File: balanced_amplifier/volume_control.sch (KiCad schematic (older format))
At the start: 49 parts, among them U5 LM4562, U6 LM4562, U7 LM4562, U8 LM4562

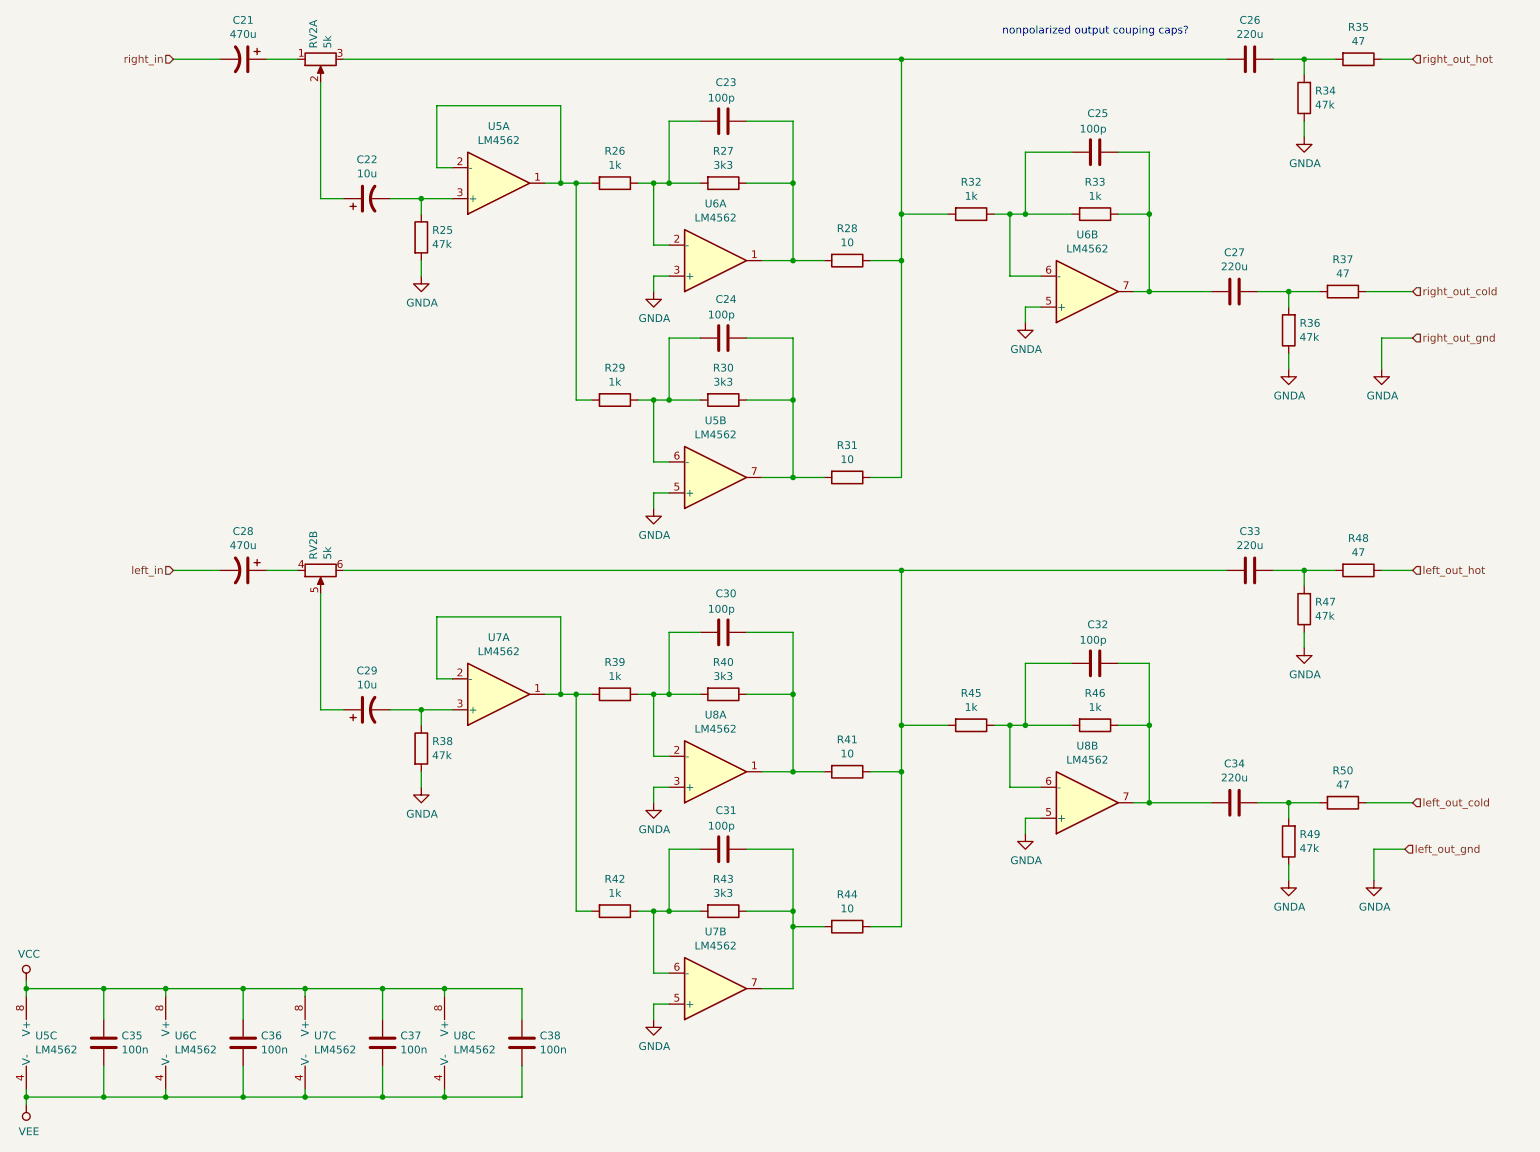
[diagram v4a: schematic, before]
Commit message: Add testpoints
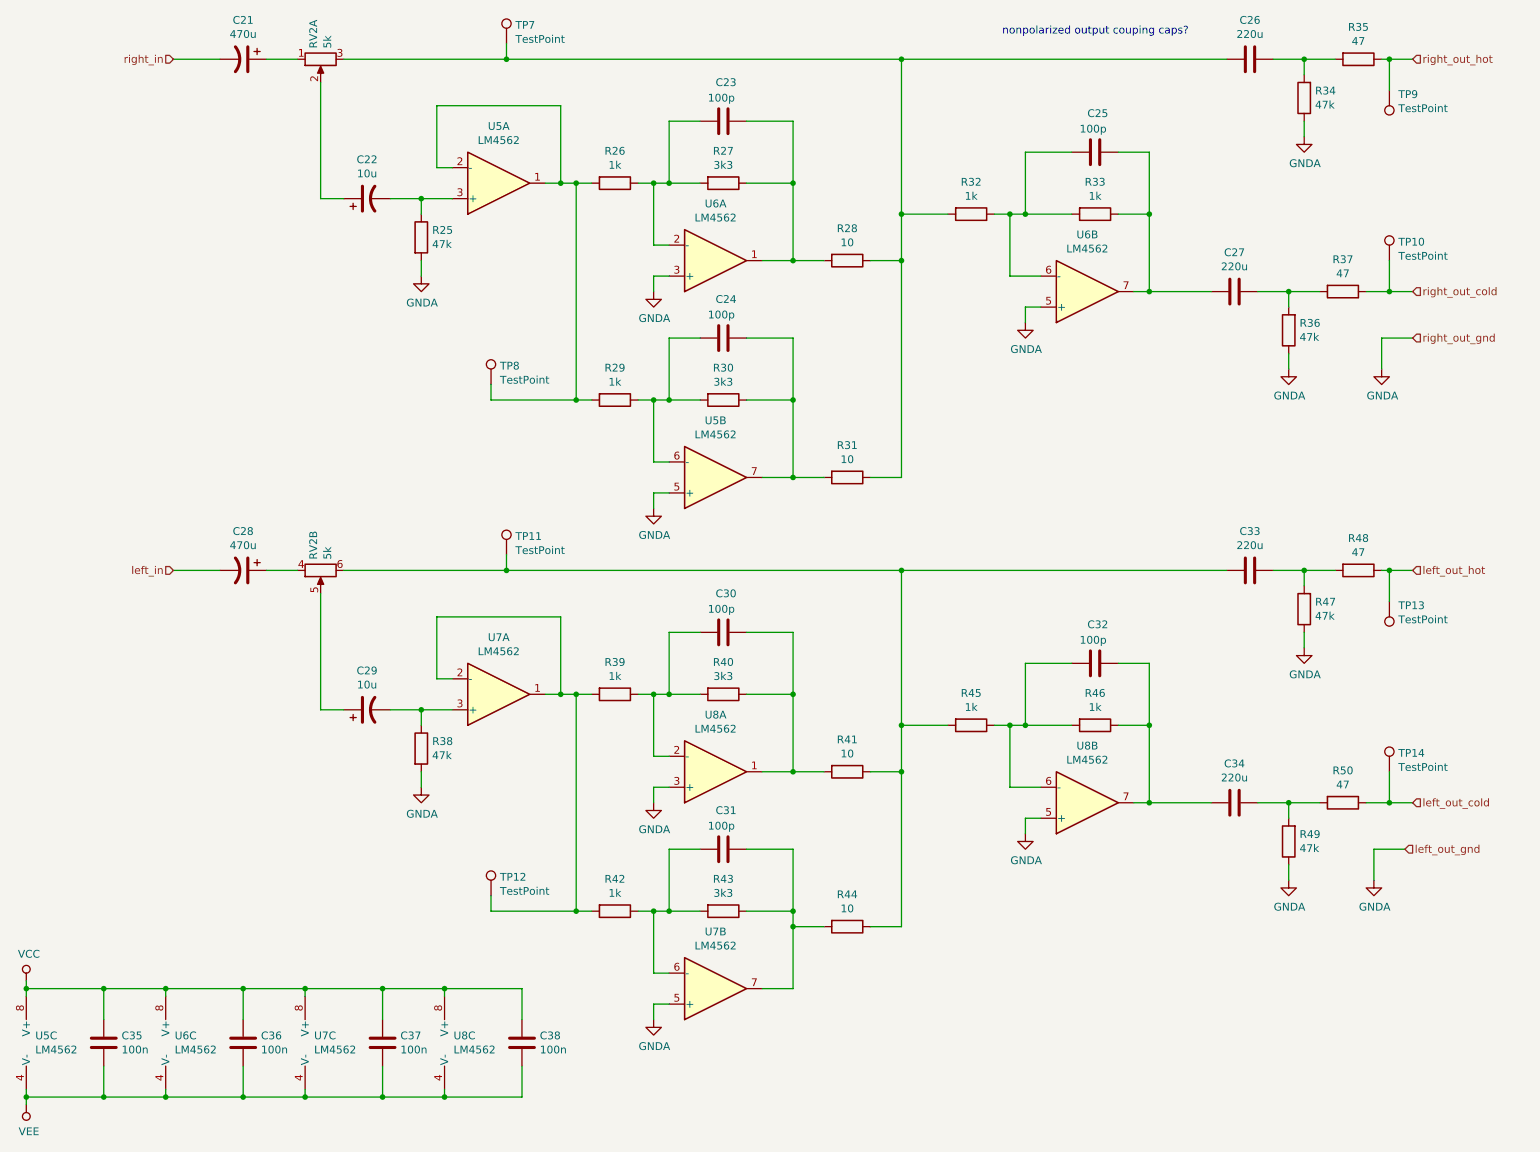
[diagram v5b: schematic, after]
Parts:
- added TP10, TP11, TP12, TP13, TP14, TP7, TP8, TP9: TestPoint, TestPoint:TestPoint_Keystone_5000-5004_Miniature, symbol Connector:TestPoint
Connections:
- net left_out_cold: now also TP14.1
- net left_out_hot: now also TP13.1
- net right_out_cold: now also TP10.1
- net right_out_hot: now also TP9.1
- net at R26.2, R29.2, U5.1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: now also TP8.1
- net at C26.2, R28.1, R31.1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: now also TP7.1
- net at R39.2, R42.2, U7.1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: now also TP12.1
- net at C33.2, R41.1, R44.1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: now also TP11.1
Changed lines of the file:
@@
 Connection ~ 8050 2400
 Wire Wire Line
-	2850 900  6450 900
+	2850 900  3900 900
 Wire Wire Line
 	6450 2200 6450 3600
@@
 left_out_gnd
 Wire Wire Line
-	9450 2400 9750 2400
+	9450 2400 9600 2400
 $Comp
 L power:GNDA #PWR?
@@
 Connection ~ 8950 5700
 Wire Wire Line
-	9450 5700 9750 5700
-Wire Wire Line
-	2850 4200 6450 4200
+	9450 5700 9600 5700
+Wire Wire Line
+	2850 4200 3900 4200
 $Comp
 L Device:R R47
@@
 Connection ~ 3500 7600
 Wire Wire Line
-	9750 900  9550 900
-Wire Wire Line
-	9750 4200 9550 4200
+	9750 900  9600 900
 Wire Wire Line
 	6450 4200 6450 5200
@@
 	0    -1   -1   0
 $EndComp
+$Comp
+L Connector:TestPoint TP?
+U 1 1 5C1B8A51
+P 3900 800
+AR Path="/5BE4EEC1/5C1B8A51" Ref="TP?"  Part="1"
+AR Path="/5BF8808C/5C1B8A51" Ref="TP7"  Part="1"
+F 0 "TP7" H 3958 920 50  0000 L CNN
+F 1 "TestPoint" H 3958 829 50  0000 L CNN
+F 2 "TestPoint:TestPoint_Keystone_5000-5004_Miniature" H 4100 800 50  0001 C CNN
+F 3 "http://www.keyelco.com/product-pdf.cfm?p=1311" H 4100 800 50  0001 C CNN
+F 4 "Keystone" H 3900 800 50  0001 C CNN "Manufacturer"
+F 5 "5002" H 3900 800 50  0001 C CNN "Manufacturer PN"
+F 6 "Digikey" H 3900 800 50  0001 C CNN "Distributor"
+F 7 "36-5002-ND" H 3900 800 50  0001 C CNN "Distributor PN"
+F 8 "https://www.digikey.com/products/en?keywords=36-5002-ND" H 3900 800 50  0001 C CNN "URL"
+F 9 "0.37" H 3900 800 50  0001 C CNN "Unit Price"
+	1    3900 800
+	1    0    0    -1
+$EndComp
+$Comp
+L Connector:TestPoint TP?
+U 1 1 5C1C3BE1
+P 3900 4100
+AR Path="/5BE4EEC1/5C1C3BE1" Ref="TP?"  Part="1"
+AR Path="/5BF8808C/5C1C3BE1" Ref="TP11"  Part="1"
+F 0 "TP11" H 3958 4220 50  0000 L CNN
+F 1 "TestPoint" H 3958 4129 50  0000 L CNN
+F 2 "TestPoint:TestPoint_Keystone_5000-5004_Miniature" H 4100 4100 50  0001 C CNN
+F 3 "http://www.keyelco.com/product-pdf.cfm?p=1311" H 4100 4100 50  0001 C CNN
+F 4 "Keystone" H 3900 4100 50  0001 C CNN "Manufacturer"
+F 5 "5002" H 3900 4100 50  0001 C CNN "Manufacturer PN"
+F 6 "Digikey" H 3900 4100 50  0001 C CNN "Distributor"
+F 7 "36-5002-ND" H 3900 4100 50  0001 C CNN "Distributor PN"
+F 8 "https://www.digikey.com/products/en?keywords=36-5002-ND" H 3900 4100 50  0001 C CNN "URL"
+F 9 "0.37" H 3900 4100 50  0001 C CNN "Unit Price"
+	1    3900 4100
+	1    0    0    -1
+$EndComp
+Wire Wire Line
+	3900 800  3900 900
+Connection ~ 3900 900
+Wire Wire Line
+	3900 900  6450 900
+Wire Wire Line
+	3900 4100 3900 4200
+Connection ~ 3900 4200
+Wire Wire Line
+	3900 4200 6450 4200
+$Comp
+L Connector:TestPoint TP?
+U 1 1 5C1DA76F
+P 3800 6300
+AR Path="/5BE4EEC1/5C1DA76F" Ref="TP?"  Part="1"
+AR Path="/5BF8808C/5C1DA76F" Ref="TP12"  Part="1"
+F 0 "TP12" H 3858 6420 50  0000 L CNN
+F 1 "TestPoint" H 3858 6329 50  0000 L CNN
+F 2 "TestPoint:TestPoint_Keystone_5000-5004_Miniature" H 4000 6300 50  0001 C CNN
+F 3 "http://www.keyelco.com/product-pdf.cfm?p=1311" H 4000 6300 50  0001 C CNN
+F 4 "Keystone" H 3800 6300 50  0001 C CNN "Manufacturer"
+F 5 "5002" H 3800 6300 50  0001 C CNN "Manufacturer PN"
+F 6 "Digikey" H 3800 6300 50  0001 C CNN "Distributor"
+F 7 "36-5002-ND" H 3800 6300 50  0001 C CNN "Distributor PN"
+F 8 "https://www.digikey.com/products/en?keywords=36-5002-ND" H 3800 6300 50  0001 C CNN "URL"
+F 9 "0.37" H 3800 6300 50  0001 C CNN "Unit Price"
+	1    3800 6300
+	1    0    0    -1
+$EndComp
+$Comp
+L Connector:TestPoint TP?
+U 1 1 5C1DA86F
+P 3800 3000
+AR Path="/5BE4EEC1/5C1DA86F" Ref="TP?"  Part="1"
+AR Path="/5BF8808C/5C1DA86F" Ref="TP8"  Part="1"
+F 0 "TP8" H 3858 3120 50  0000 L CNN
+F 1 "TestPoint" H 3858 3029 50  0000 L CNN
+F 2 "TestPoint:TestPoint_Keystone_5000-5004_Miniature" H 4000 3000 50  0001 C CNN
+F 3 "http://www.keyelco.com/product-pdf.cfm?p=1311" H 4000 3000 50  0001 C CNN
+F 4 "Keystone" H 3800 3000 50  0001 C CNN "Manufacturer"
+F 5 "5002" H 3800 3000 50  0001 C CNN "Manufacturer PN"
+F 6 "Digikey" H 3800 3000 50  0001 C CNN "Distributor"
+F 7 "36-5002-ND" H 3800 3000 50  0001 C CNN "Distributor PN"
+F 8 "https://www.digikey.com/products/en?keywords=36-5002-ND" H 3800 3000 50  0001 C CNN "URL"
+F 9 "0.37" H 3800 3000 50  0001 C CNN "Unit Price"
+	1    3800 3000
+	1    0    0    -1
+$EndComp
+Wire Wire Line
+	3800 3000 3800 3100
+Wire Wire Line
+	3800 3100 4350 3100
+Connection ~ 4350 3100
+Wire Wire Line
+	3800 6300 3800 6400
+Wire Wire Line
+	3800 6400 4350 6400
+Connection ~ 4350 6400
+$Comp
+L Connector:TestPoint TP?
+U 1 1 5C1F2A51
+P 9600 1100
+AR Path="/5BE4EEC1/5C1F2A51" Ref="TP?"  Part="1"
+AR Path="/5BF8808C/5C1F2A51" Ref="TP9"  Part="1"
+F 0 "TP9" H 9542 1127 50  0000 R CNN
+F 1 "TestPoint" H 9542 1218 50  0000 R CNN
+F 2 "TestPoint:TestPoint_Keystone_5000-5004_Miniature" H 9800 1100 50  0001 C CNN
+F 3 "http://www.keyelco.com/product-pdf.cfm?p=1311" H 9800 1100 50  0001 C CNN
+F 4 "Keystone" H 9600 1100 50  0001 C CNN "Manufacturer"
+F 5 "5002" H 9600 1100 50  0001 C CNN "Manufacturer PN"
+F 6 "Digikey" H 9600 1100 50  0001 C CNN "Distributor"
+F 7 "36-5002-ND" H 9600 1100 50  0001 C CNN "Distributor PN"
+F 8 "https://www.digikey.com/products/en?keywords=36-5002-ND" H 9600 1100 50  0001 C CNN "URL"
+F 9 "0.37" H 9600 1100 50  0001 C CNN "Unit Price"
+	1    9600 1100
+	-1   0    0    1
+$EndComp
+$Comp
+L Connector:TestPoint TP?
+U 1 1 5C1F2BD1
+P 9600 2200
+AR Path="/5BE4EEC1/5C1F2BD1" Ref="TP?"  Part="1"
+AR Path="/5BF8808C/5C1F2BD1" Ref="TP10"  Part="1"
+F 0 "TP10" H 9658 2320 50  0000 L CNN
+F 1 "TestPoint" H 9658 2229 50  0000 L CNN
+F 2 "TestPoint:TestPoint_Keystone_5000-5004_Miniature" H 9800 2200 50  0001 C CNN
+F 3 "http://www.keyelco.com/product-pdf.cfm?p=1311" H 9800 2200 50  0001 C CNN
+F 4 "Keystone" H 9600 2200 50  0001 C CNN "Manufacturer"
+F 5 "5002" H 9600 2200 50  0001 C CNN "Manufacturer PN"
+F 6 "Digikey" H 9600 2200 50  0001 C CNN "Distributor"
+F 7 "36-5002-ND" H 9600 2200 50  0001 C CNN "Distributor PN"
+F 8 "https://www.digikey.com/products/en?keywords=36-5002-ND" H 9600 2200 50  0001 C CNN "URL"
+F 9 "0.37" H 9600 2200 50  0001 C CNN "Unit Price"
+	1    9600 2200
+	1    0    0    -1
+$EndComp
+Wire Wire Line
+	9600 1100 9600 900
+Connection ~ 9600 900
+Wire Wire Line
+	9600 900  9550 900
+Wire Wire Line
+	9600 2200 9600 2400
+Connection ~ 9600 2400
+Wire Wire Line
+	9600 2400 9750 2400
+$Comp
+L Connector:TestPoint TP?
+U 1 1 5C20B57F
+P 9600 5500
+AR Path="/5BE4EEC1/5C20B57F" Ref="TP?"  Part="1"
+AR Path="/5BF8808C/5C20B57F" Ref="TP14"  Part="1"
+F 0 "TP14" H 9658 5620 50  0000 L CNN
+F 1 "TestPoint" H 9658 5529 50  0000 L CNN
+F 2 "TestPoint:TestPoint_Keystone_5000-5004_Miniature" H 9800 5500 50  0001 C CNN
+F 3 "http://www.keyelco.com/product-pdf.cfm?p=1311" H 9800 5500 50  0001 C CNN
+F 4 "Keystone" H 9600 5500 50  0001 C CNN "Manufacturer"
+F 5 "5002" H 9600 5500 50  0001 C CNN "Manufacturer PN"
+F 6 "Digikey" H 9600 5500 50  0001 C CNN "Distributor"
+F 7 "36-5002-ND" H 9600 5500 50  0001 C CNN "Distributor PN"
+F 8 "https://www.digikey.com/products/en?keywords=36-5002-ND" H 9600 5500 50  0001 C CNN "URL"
+F 9 "0.37" H 9600 5500 50  0001 C CNN "Unit Price"
+	1    9600 5500
+	1    0    0    -1
+$EndComp
+$Comp
+L Connector:TestPoint TP?
+U 1 1 5C20B862
+P 9600 4400
+AR Path="/5BE4EEC1/5C20B862" Ref="TP?"  Part="1"
+AR Path="/5BF8808C/5C20B862" Ref="TP13"  Part="1"
+F 0 "TP13" H 9542 4427 50  0000 R CNN
+F 1 "TestPoint" H 9542 4518 50  0000 R CNN
+F 2 "TestPoint:TestPoint_Keystone_5000-5004_Miniature" H 9800 4400 50  0001 C CNN
+F 3 "http://www.keyelco.com/product-pdf.cfm?p=1311" H 9800 4400 50  0001 C CNN
+F 4 "Keystone" H 9600 4400 50  0001 C CNN "Manufacturer"
+F 5 "5002" H 9600 4400 50  0001 C CNN "Manufacturer PN"
+F 6 "Digikey" H 9600 4400 50  0001 C CNN "Distributor"
+F 7 "36-5002-ND" H 9600 4400 50  0001 C CNN "Distributor PN"
+F 8 "https://www.digikey.com/products/en?keywords=36-5002-ND" H 9600 4400 50  0001 C CNN "URL"
+F 9 "0.37" H 9600 4400 50  0001 C CNN "Unit Price"
+	1    9600 4400
+	-1   0    0    1
+$EndComp
+Wire Wire Line
+	9600 4400 9600 4200
+Wire Wire Line
+	9550 4200 9600 4200
+Connection ~ 9600 4200
+Wire Wire Line
+	9600 4200 9750 4200
+Wire Wire Line
+	9600 5500 9600 5700
+Connection ~ 9600 5700
+Wire Wire Line
+	9600 5700 9750 5700
 $EndSCHEMATC
